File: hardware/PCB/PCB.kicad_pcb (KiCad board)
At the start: 2 copper layers, 34.1 x 57.9 mm, 25 parts, among them IC1 TSS721ADR, J1 Conn_01x02_Pin, J2 USB_C_Receptacle_USB2.0_14P, SW1 SW_Push, SW2 SW_Push, U1 ESP32-C6-MINI-1, U3 MCP1700x-330xxTT

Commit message: Finished initial schematic and PCB
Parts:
- removed IC1: TSS721ADR, Package_SO:SOIC-16_3.9x9.9mm_P1.27mm
- removed R1, R2: 220, Resistor_SMD:R_0805_2012Metric
- added C10: 1µF, Capacitor_SMD:C_0805_2012Metric, F.Cu at (133.8, 49.8)
- added C6: 4.7µF, Capacitor_SMD:C_0805_2012Metric, F.Cu at (136.1, 68.6)
- added C9: 10µF, Capacitor_SMD:C_0805_2012Metric, F.Cu at (137.9, 55.1)
- added D4: SS14, Diode_SMD:D_SMA, F.Cu at (133.6, 54.6)
- added F1: Polyfuse, Inductor_SMD:L_1206_3216Metric_Pad1.22x1.90mm_HandSolder, F.Cu at (139.2, 69.2)
- added L2: 10uH, CR54NP-100MC:CR54NP221KC, F.Cu at (135.8, 62.4)
- added Q1: BC807, Package_TO_SOT_SMD:SOT-23, F.Cu at (152.4, 48.8)
- added Q2: BC817, Package_TO_SOT_SMD:SOT-23, F.Cu at (152.4, 56.6)
- added Q3: BC817, Package_TO_SOT_SMD:SOT-23, F.Cu at (158.0, 53.1)
- added R11: 37K, Resistor_SMD:R_0805_2012Metric, F.Cu at (141.2, 55.1)
- added R12: 39K, Resistor_SMD:R_0805_2012Metric, F.Cu at (149.1, 51.8)
- added R13: 33K, Resistor_SMD:R_0805_2012Metric, F.Cu at (157.7, 57.9)
- added R14: 220K, Resistor_SMD:R_0805_2012Metric, F.Cu at (138.9, 50.0)
- added R15: 82, Resistor_SMD:R_0805_2012Metric, F.Cu at (158.0, 48.5)
- added R16: 1K, Resistor_SMD:R_0805_2012Metric, F.Cu at (157.7, 65.5)
- added R17: 1K, Resistor_SMD:R_0805_2012Metric, F.Cu at (157.7, 69.1)
- added R19: 22K, Resistor_SMD:R_0805_2012Metric, F.Cu at (153.4, 53.6)
- added R20: 3K3, Resistor_SMD:R_0805_2012Metric, F.Cu at (157.7, 61.7)
- added U2: AP3015, Package_TO_SOT_SMD:SOT-23-5, F.Cu at (144.8, 51.6)
- C2: value 10µ -> 22µ
- J1: footprint Connector_PinSocket_2.54mm:PinSocket_1x02_P2.54mm_Vertical -> TerminalBlock:TerminalBlock_MaiXu_MX126-5.0-02P_1x02_P5.00mm
- R10: value 100 -> 1M
- U1: footprint RF_Module:ESP32-C6-MINI-1 -> PCM_Espressif:ESP32-C6-MINI-1U
- moved R8 73.7 mm to (153.0, 74.7)
- moved R7 72.4 mm to (153.0, 76.8)
- moved R6 71.4 mm to (153.0, 78.9)
- moved D3 69.5 mm to (157.0, 74.7), turned to 180 degrees
- moved D2 67.9 mm to (156.9, 76.8), turned to 180 degrees
- moved D1 66.7 mm to (156.9, 78.9), turned to 180 degrees
- moved R3 66.5 mm to (148.9, 77.2), turned to 90 degrees
- moved U3 65.1 mm to (142.0, 77.2), turned to -90 degrees
- moved SW2 62.0 mm to (158.2, 86.3), turned to 90 degrees
- moved R9 61.4 mm to (145.7, 73.6)
- moved C7 60.7 mm to (145.4, 77.2), turned to 90 degrees
- moved R4 57.0 mm to (139.3, 79.6), turned to 180 degrees
- moved C3 52.8 mm to (138.4, 75.7), turned to 90 degrees
- moved R5 52.3 mm to (134.2, 79.0), turned to 180 degrees
- moved U1 51.8 mm to (148.5, 63.2), turned to 0 degrees
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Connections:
- J1 pad 1: unconnected-(J1-Pin_1-Pad1) -> MBUS+
- J1 pad 2: unconnected-(J1-Pin_2-Pad2) -> MBUS-
- J2 pad SH: (no net) -> GND
- R10 pad 1: Net-(IC1-RIS) -> MBUS+
- R10 pad 2: GND -> Net-(U2-FB)
- U1 pad 20: unconnected-(U1-IO15-Pad20) -> LED
- U1 pad 27: LED -> unconnected-(U1-IO21-Pad27)
- U1 pad 28: unconnected-(U1-IO22-Pad28) -> UART1_RX
- U1 pad 29: unconnected-(U1-IO23-Pad29) -> UART1_TX
- U1 pad 30: unconnected-(U1-RXD0-Pad30) -> UART0_RX
- U1 pad 31: unconnected-(U1-TXD0-Pad31) -> UART0_TX
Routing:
- net GND: track 0.00 -> 132.9 mm, vias 0 -> 8
- net MBUS+: track 0.00 -> 49.1 mm
- net +3.3V: track 0.00 -> 40.6 mm, vias 0 -> 2
- net Net-(U2-IN): track 0.00 -> 27.1 mm, vias 0 -> 4
- net +5V: track 0.00 -> 24.2 mm, vias 0 -> 2
- net EN: track 0.00 -> 21.9 mm, vias 0 -> 2
- net MBUS-: track 0.00 -> 18.9 mm
- net BOOT: track 0.00 -> 16.5 mm, vias 0 -> 2
- net Net-(Q3-C): track 0.00 -> 16.1 mm
- net USB_D+: track 0.00 -> 15.3 mm, vias 0 -> 2
- net USB_D-: track 0.00 -> 14.8 mm, vias 0 -> 2
- net Net-(Q2-B): track 0.00 -> 11.2 mm, vias 0 -> 2
- net Net-(Q1-B): track 0.00 -> 10.9 mm
- net Net-(Q1-E): track 0.00 -> 10.2 mm
- net GPIO8: track 0.00 -> 9.65 mm, vias 0 -> 2
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- added copper zone on B.Cu, net GND
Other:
- board size 34.1 x 57.9 mm -> 29.6 x 50.8 mm

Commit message: Finish BOMed and made some pad size adjustments for higher voltage tracks
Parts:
- C10, C6, C9: footprint Capacitor_SMD:C_0805_2012Metric -> Capacitor_SMD:C_1206_3216Metric
- moved C6 0.58 mm to (136.1, 69.1)
- moved C10 0.57 mm to (134.4, 49.8)
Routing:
- net GND: track 132.9 -> 132.2 mm

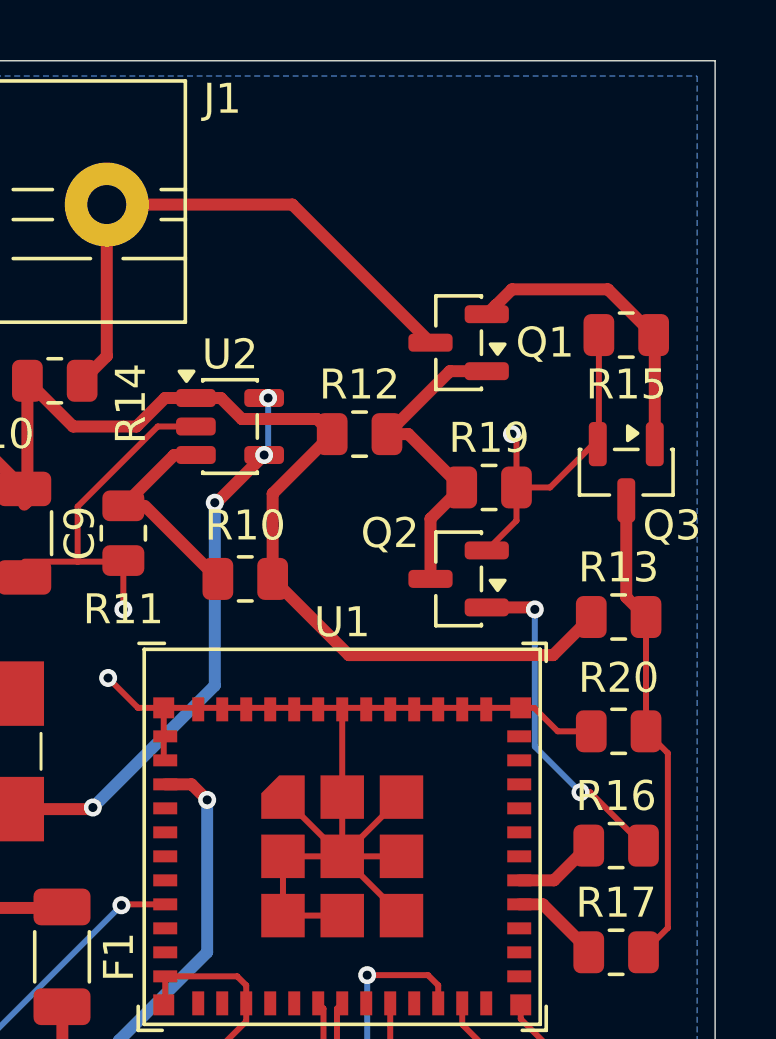
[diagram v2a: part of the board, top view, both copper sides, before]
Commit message: Add debugging header
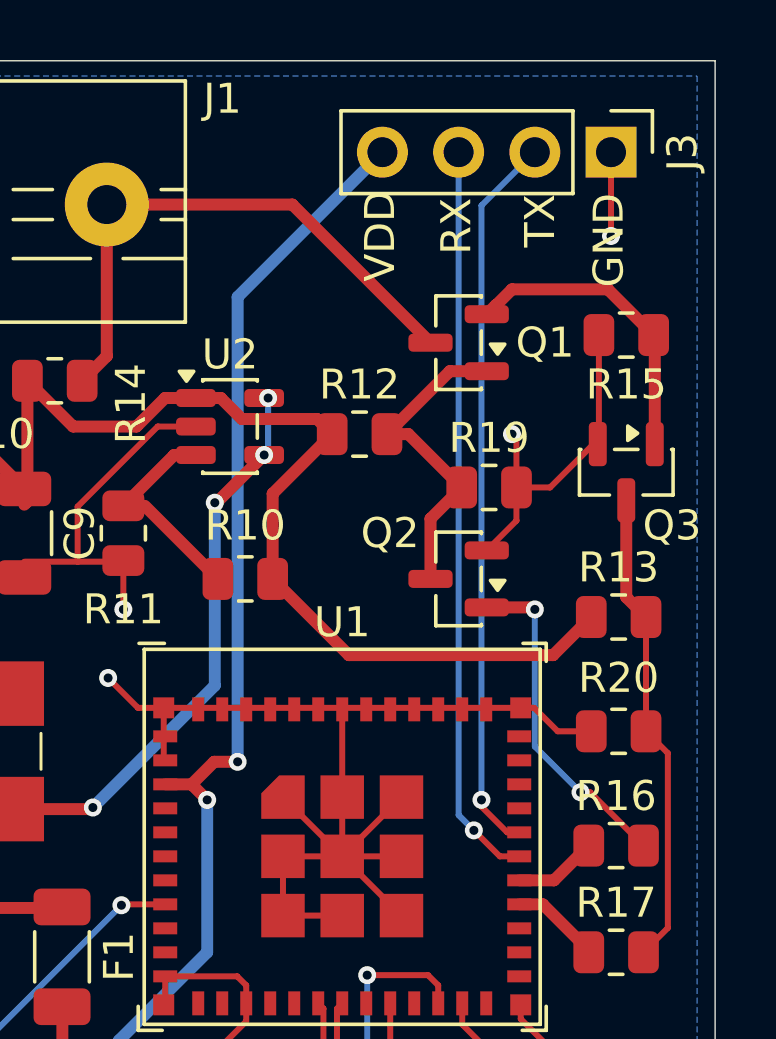
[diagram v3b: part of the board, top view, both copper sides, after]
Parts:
- added J3: Conn_01x04_Pin, Connector_PinHeader_2.54mm:PinHeader_1x04_P2.54mm_Vertical, F.Cu at (157.5, 42.4)
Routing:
- net UART0_RX: track 0.00 -> 24.7 mm, vias 0 -> 1
- net +3.3V: track 40.6 -> 64.8 mm, vias 2 -> 3
- net UART0_TX: track 0.00 -> 24.2 mm, vias 0 -> 1
- net GND: track 132.2 -> 135.0 mm, vias 8 -> 9
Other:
- board text added: "GND"
- board text added: "RX"
- board text added: "TX"
- board text added: "VDD"
